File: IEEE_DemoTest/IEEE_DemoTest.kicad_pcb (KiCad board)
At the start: 2 copper layers, 98.9 x 105.3 mm, 1 part

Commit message: changed demo
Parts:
- added 3V1: Battery_Cell, IEEEOrnamentupdate1:CR2025TR, B.Cu at (132.3, 92.1)
- added C1: 0.01uF, Capacitor_THT:CP_Radial_D5.0mm_P2.00mm, F.Cu at (144.7, 108.7)
- added C2: 10uf, Capacitor_THT:CP_Radial_D5.0mm_P2.00mm, F.Cu at (159.4, 94.1)
- added D1: LED, IEEEOrnamentupdate1:IN-S63AT, F.Cu at (129.1, 107.9)
- added D2: LED, IEEEOrnamentupdate1:IN-S63AT, F.Cu at (142.1, 113.3)
- added D3: LED, IEEEOrnamentupdate1:IN-S63AT, F.Cu at (170.7, 86.5)
- added D4: LED, IEEEOrnamentupdate1:IN-S63AT, F.Cu at (150.8, 106.8)
- added D5: LED, IEEEOrnamentupdate1:IN-S63AT, F.Cu at (171.3, 84.0)
- added D6: LED, IEEEOrnamentupdate1:IN-S63AT, F.Cu at (167.0, 86.5)
- added D7: LED, IEEEOrnamentupdate1:IN-S63AT, F.Cu at (137.8, 110.8)
- added D8: LED, IEEEOrnamentupdate1:IN-S63AT, F.Cu at (167.0, 88.8)
- added D9: LED, IEEEOrnamentupdate1:IN-S63AT, F.Cu at (158.8, 98.7)
- added R1: 1k, Resistor_THT:R_Axial_DIN0207_L6.3mm_D2.5mm_P7.62mm_Horizontal, F.Cu at (133.2, 107.5)
- added R10: 100, Resistor_SMD:R_0603_1608Metric_Pad0.98x0.95mm_HandSolder, F.Cu at (138.1, 102.7)
- added R2: 100, Resistor_SMD:R_0603_1608Metric_Pad0.98x0.95mm_HandSolder, F.Cu at (129.5, 113.3)
- added R3: 100, Resistor_SMD:R_0603_1608Metric_Pad0.98x0.95mm_HandSolder, F.Cu at (133.9, 113.3)
- added R4: 100, Resistor_SMD:R_0603_1608Metric_Pad0.98x0.95mm_HandSolder, F.Cu at (142.5, 102.7)
- added R5: 100, Resistor_SMD:R_0603_1608Metric_Pad0.98x0.95mm_HandSolder, F.Cu at (167.4, 83.9)
- added R6: 100, Resistor_SMD:R_0603_1608Metric_Pad0.98x0.95mm_HandSolder, F.Cu at (133.8, 102.7)
- added R7: 100, Resistor_SMD:R_0603_1608Metric_Pad0.98x0.95mm_HandSolder, F.Cu at (129.5, 110.8)
- added R8: 100, Resistor_SMD:R_0603_1608Metric_Pad0.98x0.95mm_HandSolder, F.Cu at (138.2, 113.2)
- added R9: 100, Resistor_SMD:R_0603_1608Metric_Pad0.98x0.95mm_HandSolder, F.Cu at (133.9, 110.8)
- added RV1: R_Potentiometer_US, IEEEOrnamentupdate1:CT6EP504, F.Cu at (161.1, 86.7)
- added SW1: SW_DPDT_x2, IEEEOrnamentupdate1:EG1218, F.Cu at (125.3, 104.0)
- added U1: LM555xM, Package_SO:SOIC-8_3.9x4.9mm_P1.27mm, F.Cu at (123.1, 109.8)
- added U2: 4017, IEEEOrnamentupdate1:4017, F.Cu at (148.1, 84.5)

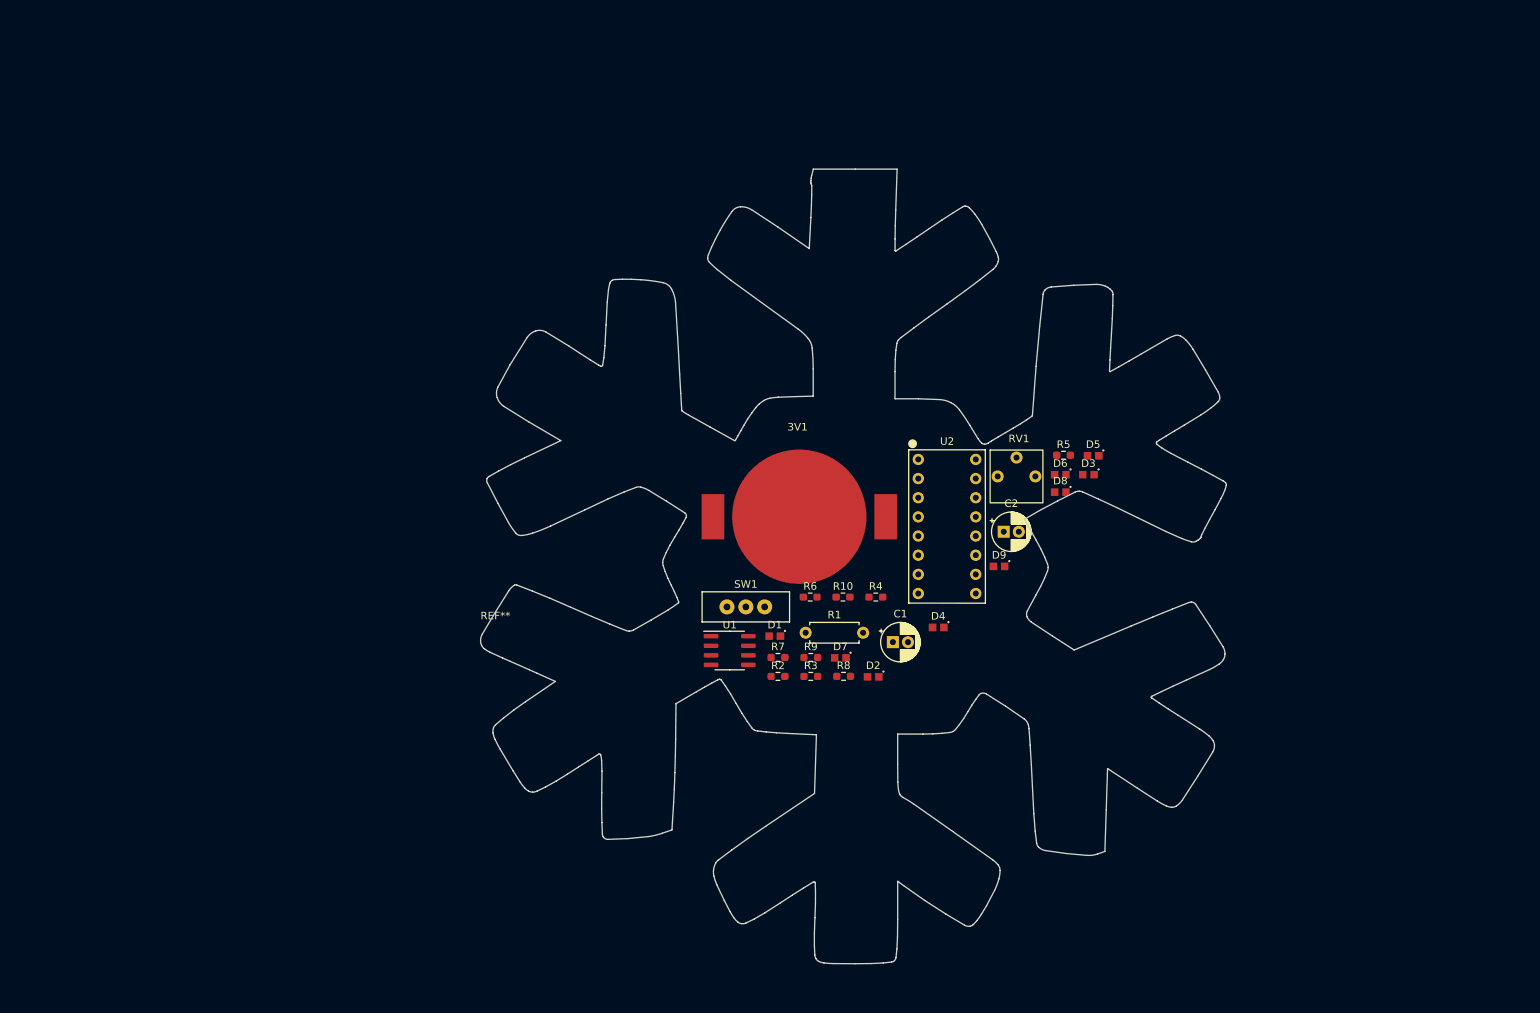
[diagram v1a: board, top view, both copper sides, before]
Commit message: update schematic, pot footprint
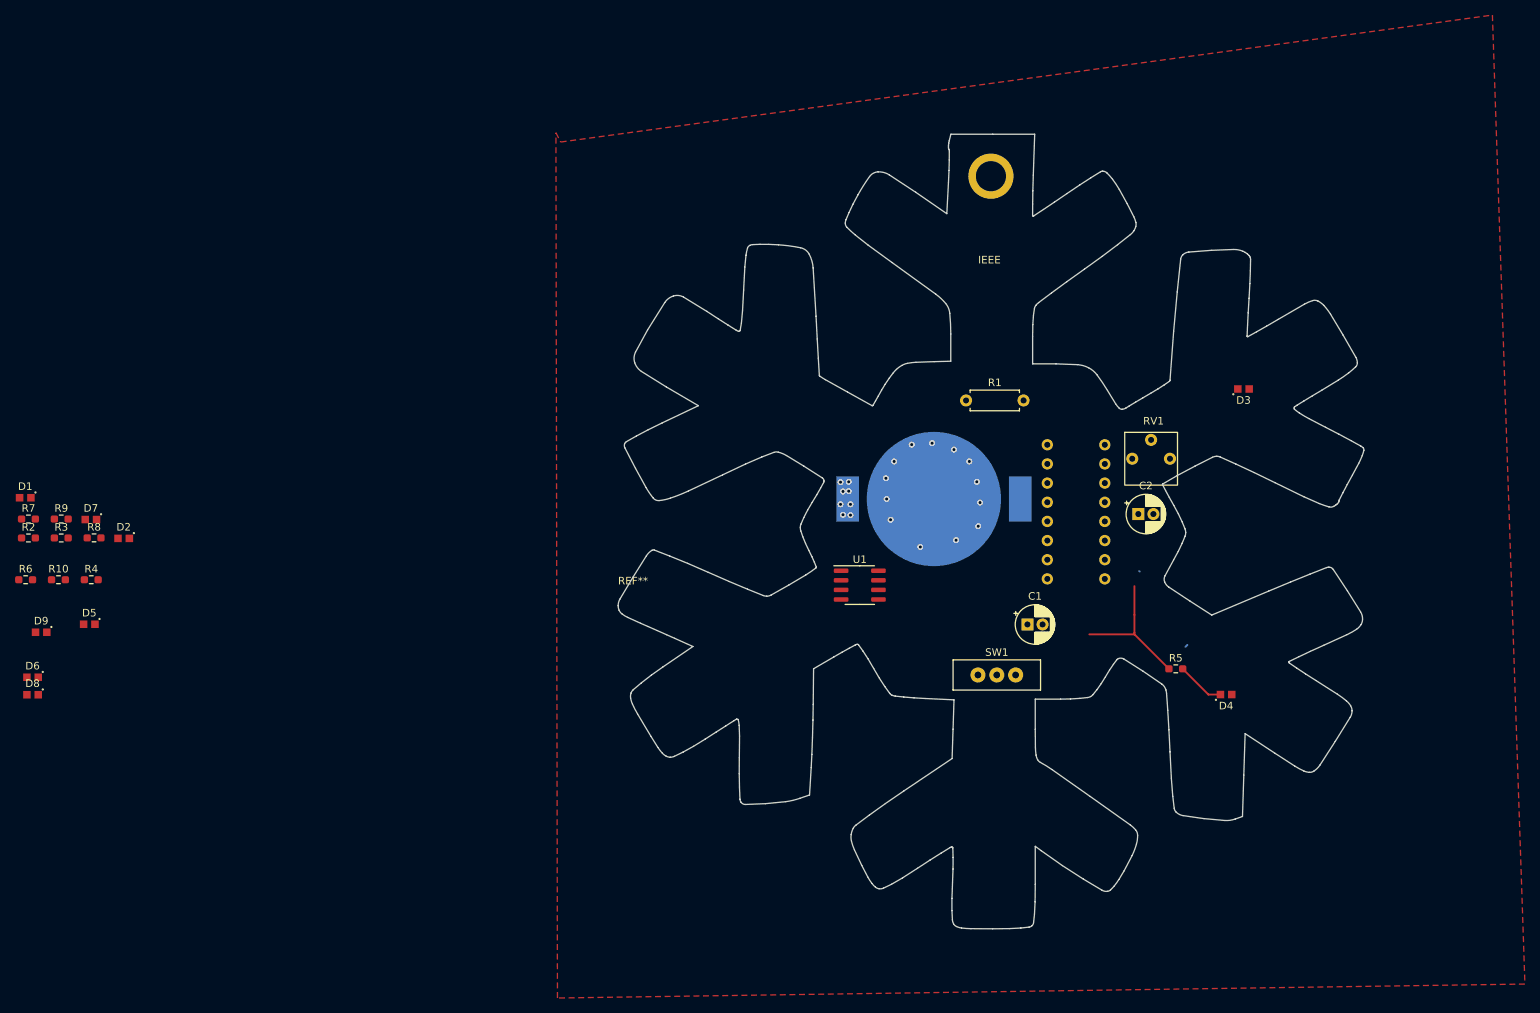
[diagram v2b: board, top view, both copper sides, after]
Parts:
- removed the REF** at (92.1, 104.7)
- added REF**: Snowflake, IEEEOrnamentupdate2:Snowflake, F.Cu at (110.3, 100.1)
- 3V1: moved to F.Cu
- U2: moved to B.Cu
- moved D6 138.9 mm to (30.7, 113.4)
- moved D8 138.9 mm to (30.7, 115.7)
- moved D5 135.0 mm to (38.2, 106.3)
- moved D9 127.3 mm to (31.8, 107.4)
- moved R4 104.0 mm to (38.5, 100.4)
- moved R10 104.0 mm to (34.1, 100.4)
- moved R6 104.0 mm to (29.8, 100.4)
- moved R2 101.1 mm to (30.1, 94.9)
- moved R7 101.1 mm to (30.1, 92.4)
- moved D1 101.1 mm to (29.7, 89.6)
- moved D2 101.1 mm to (42.8, 95.0)
- moved R3 101.1 mm to (34.5, 94.9)
- moved R8 101.1 mm to (38.8, 94.9)
- moved R9 101.1 mm to (34.5, 92.4)
- moved D7 101.1 mm to (38.4, 92.5)
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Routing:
- net Net-(R5-Pad1): track 0.00 -> 18.9 mm
- net Net-(D4-Pad2): track 0.00 -> 6.42 mm
- net GND: track 0.00 -> 0.37 mm, vias 0 -> 13
- net Net-(3V1-Pad1): vias 0 -> 8
- added copper zone on F.Cu, net GND
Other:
- outline, holes or cut-outs redrawn
- board text added: "IEEE"
